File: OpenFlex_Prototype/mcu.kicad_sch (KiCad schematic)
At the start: 1 part, among them U5 ESP32-S2-DEVKITC-1

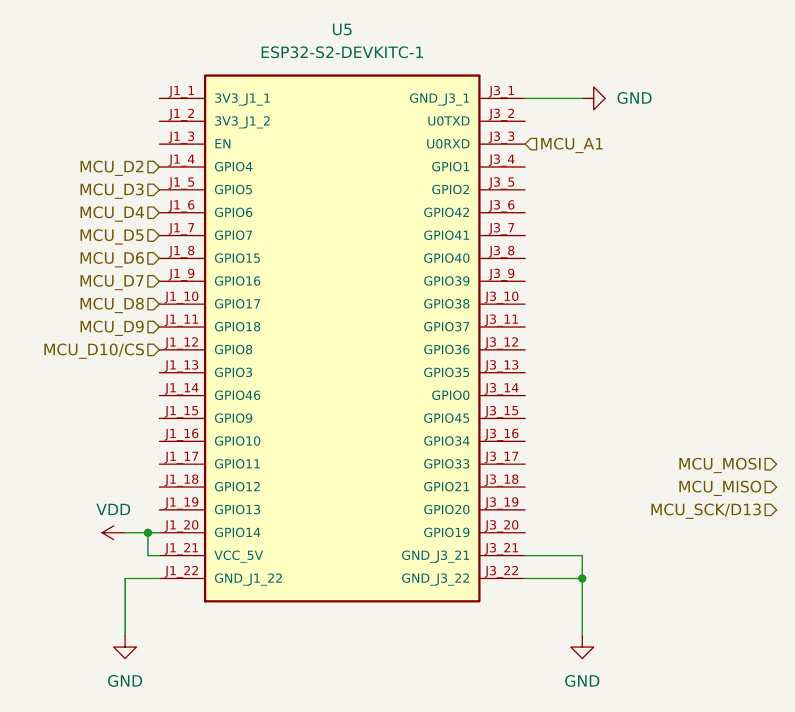
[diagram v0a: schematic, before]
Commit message: Updated PCB to ESP32-S2-Devkit-C1
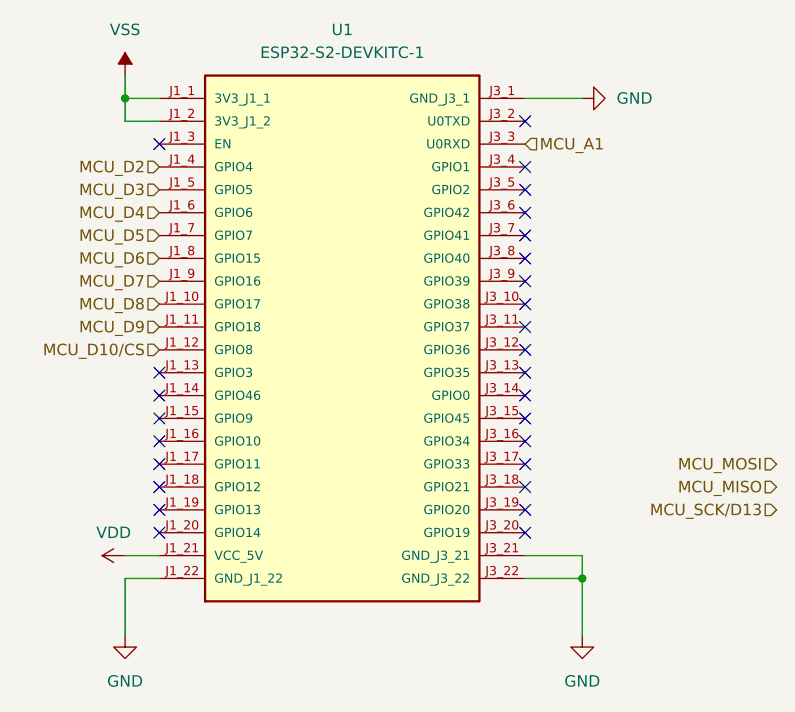
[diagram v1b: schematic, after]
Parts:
- renumbered U5 to U1
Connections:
- net VDD: no longer U1.J1_20 (GPIO14)
- net VSS: now reaches U1.J1_1 (3V3_J1_1)
- net VSS: now also U1.J1_2 (3V3_J1_2)
- no-connect marks 0 -> 27
